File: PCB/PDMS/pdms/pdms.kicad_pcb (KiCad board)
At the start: 2 copper layers, 152 parts, among them IC1 BTS500101TAEATMA1, IC12 TMP126NDCKR, IC13 TMP126NDCKR, IC14 TMP126NDCKR, IC15 LM74700QDBVRQ1, IC16 BTS722204ESAXUMA1, IC2 BTS500101TAEATMA1, IC3 BTS500101TAEATMA1, IC4 BTS500101TAEATMA1, IC5 BTS500101TAEATMA1, IC6 BTS500101TAEATMA1, IC7 BTS722204ESAXUMA1, IC8 BTS500101TAEATMA1, IC9 BTS500101TAEATMA1, J1 DBG, Q1 AO3401A, Q2 MMBT3904, Q3 IAUA250N04S6N007AUMA1, U1 STM32F405RGTx, U2 MCP2561-E-SN, U3 MCP2561-E-SN, Y1 16Mhz, Y2 32KHz

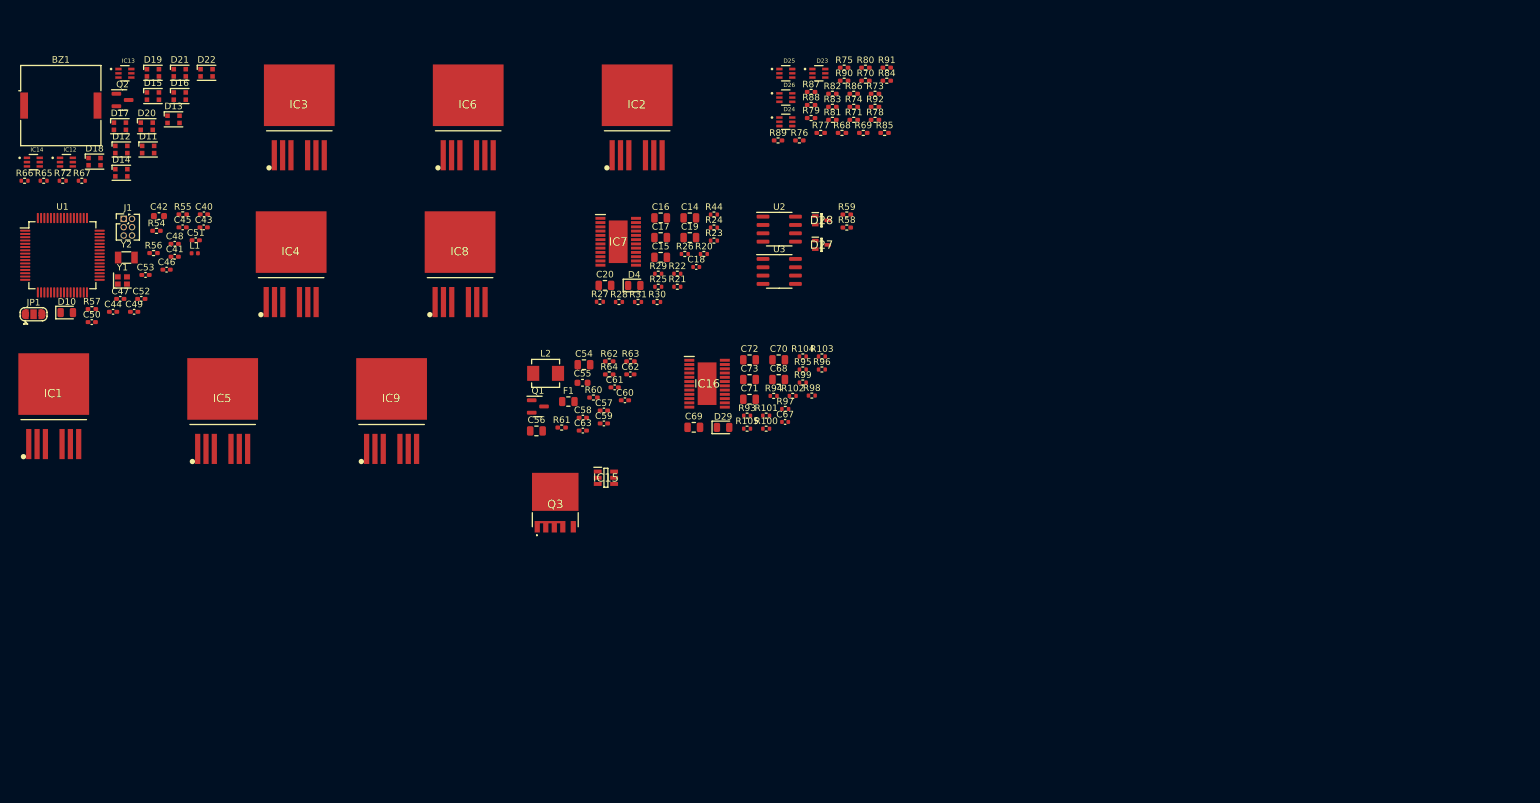
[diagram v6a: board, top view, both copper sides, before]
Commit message: Changed MCU to L496 & finished powerswitch section
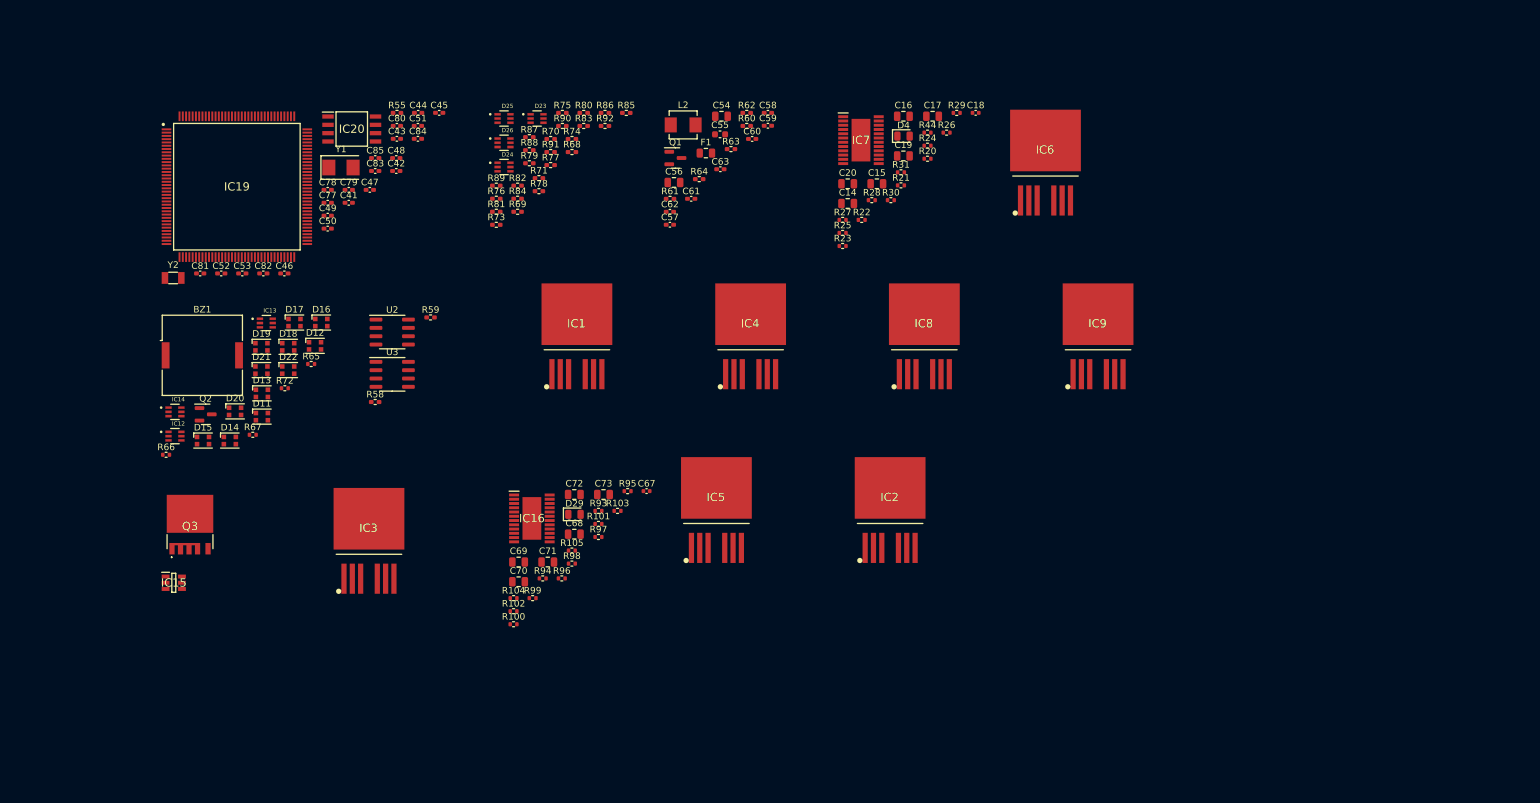
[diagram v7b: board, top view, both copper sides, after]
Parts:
- removed C40: 2u2, Capacitor_SMD:C_0402_1005Metric_Pad0.74x0.62mm_HandSolder
- removed D10: LED_Small, LED_SMD:LED_0805_2012Metric
- removed D27, D28: PESD2CANFD24L-UX, PDMS_Additional:SOT65P210X110-3N
- removed J1: DBG, Connector_PinHeader_1.27mm:PinHeader_2x03_P1.27mm_Vertical
- removed JP1: SolderJumper_3_Open, Jumper:SolderJumper-3_P1.3mm_Open_RoundedPad1.0x1.5mm
- removed L1: 2u7 120m, Inductor_SMD:L_0402_1005Metric
- removed R54: 2k2, Resistor_SMD:R_0402_1005Metric_Pad0.72x0.64mm_HandSolder
- removed R56: 1k5, Resistor_SMD:R_0402_1005Metric_Pad0.72x0.64mm_HandSolder
- removed R57: 1k, Resistor_SMD:R_0402_1005Metric_Pad0.72x0.64mm_HandSolder
- removed U1: STM32F405RGTx, Package_QFP:LQFP-64_10x10mm_P0.5mm
- added C77: 100n, Capacitor_SMD:C_0402_1005Metric_Pad0.74x0.62mm_HandSolder, F.Cu at (69.9, 42.8)
- added C78: 100n, Capacitor_SMD:C_0402_1005Metric_Pad0.74x0.62mm_HandSolder, F.Cu at (69.9, 40.8)
- added C79: 100n, Capacitor_SMD:C_0402_1005Metric_Pad0.74x0.62mm_HandSolder, F.Cu at (73.1, 40.8)
- added C80: 100n, Capacitor_SMD:C_0402_1005Metric_Pad0.74x0.62mm_HandSolder, F.Cu at (80.5, 31.0)
- added C81: 100n, Capacitor_SMD:C_0402_1005Metric_Pad0.74x0.62mm_HandSolder, F.Cu at (50.5, 53.5)
- added C82: 100n, Capacitor_SMD:C_0402_1005Metric_Pad0.74x0.62mm_HandSolder, F.Cu at (60.1, 53.5)
- added C83: 1u, Capacitor_SMD:C_0402_1005Metric_Pad0.74x0.62mm_HandSolder, F.Cu at (77.2, 37.9)
- added C84: 10pF, Capacitor_SMD:C_0402_1005Metric_Pad0.74x0.62mm_HandSolder, F.Cu at (83.7, 33.0)
- added C85: 10pF, Capacitor_SMD:C_0402_1005Metric_Pad0.74x0.62mm_HandSolder, F.Cu at (77.2, 36.0)
- added IC19: STM32L496ZGT6, PDM_Additional:QFP50P2200X2200X160-144N, F.Cu at (56.1, 40.3)
- added IC20: AT25SF128A-SHB-T, PDM_Additional:SOIC127P798X216-8N, F.Cu at (73.6, 31.5)
- C41: value 2u2 -> 4u7
- C42: value 4,7uF -> 10pF; footprint Capacitor_SMD:C_0603_1608Metric -> Capacitor_SMD:C_0402_1005Metric_Pad0.74x0.62mm_HandSolder
- C43: value 100nF -> 1u
- C44, C45: value 100nF -> 100n
- C46: value 100nF -> 10pF
- C48, C50, C52, C53: value 10pF -> 100n
- C51: value 1u -> 100n
- R55: value 2k2 -> 1k
- Y1: value 16Mhz -> 48Mhz; footprint Crystal:Crystal_SMD_2016-4Pin_2.0x1.6mm -> Crystal:Crystal_SMD_5032-2Pin_5.0x3.2mm
- moved IC9 108.4 mm to (187.4, 59.8)
- moved IC6 88.3 mm to (179.4, 33.3)
- moved IC1 80.5 mm to (107.9, 59.8)
- moved IC5 76.8 mm to (129.2, 86.3)
- moved R58 76.7 mm to (77.2, 73.2)
- moved IC8 71.7 mm to (160.9, 59.8)
- moved IC2 71.3 mm to (155.7, 86.3)
- moved IC4 70.9 mm to (134.4, 59.8)
- moved IC15 67.8 mm to (46.4, 100.7)
- moved IC3 65.5 mm to (76.2, 91.0)
- moved R59 65.4 mm to (85.6, 60.3)
- moved R73 61.1 mm to (95.6, 46.1)
- moved U2 61.1 mm to (79.8, 62.5)
- moved U3 61.1 mm to (79.8, 68.9)
- moved R84 59.1 mm to (98.9, 42.1)
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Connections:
- net /POWER_SWITCHES/BTS50010-1TAE/MOS_OUT renamed HP_MOS1
- net /POWER_SWITCHES/BTS50010-1TAE1/MOS_OUT renamed HP_MOS2
- net /POWER_SWITCHES/BTS50010-1TAE2/MOS_OUT renamed HP_MOS3
- net /POWER_SWITCHES/BTS50010-1TAE3/MOS_OUT renamed HP_MOS4
- net /POWER_SWITCHES/BTS50010-1TAE4/MOS_OUT renamed HP_MOS5
- net /POWER_SWITCHES/BTS50010-1TAE6/MOS_OUT renamed HP_MOS6
- net /POWER_SWITCHES/BTS722204/ADC renamed SENS_OUT_LP1
- net /POWER_SWITCHES/BTS722204/IN0 renamed LP_SIG_IN1
- net /POWER_SWITCHES/BTS722204/IN1 renamed LP_SIG_IN2
- net /POWER_SWITCHES/BTS722204/IN2 renamed LP_SIG_IN3
- net /POWER_SWITCHES/BTS722204/IN3 renamed LP_SIG_IN4
- net /POWER_SWITCHES/BTS722204/OUT0 renamed LP_MOS1
- net /POWER_SWITCHES/BTS722204/OUT1 renamed LP_MOS2
- net /POWER_SWITCHES/BTS722204/OUT2 renamed LP_MOS3
- net /POWER_SWITCHES/BTS722204/OUT3 renamed LP_MOS4
- net /POWER_SWITCHES/BTS722205/ADC renamed SENS_OUT_LP2
- net /POWER_SWITCHES/BTS722205/IN0 renamed LP_SIG_IN5
- net /POWER_SWITCHES/BTS722205/IN1 renamed LP_SIG_IN6
- net /POWER_SWITCHES/BTS722205/IN2 renamed LP_SIG_IN7
- net /POWER_SWITCHES/BTS722205/IN3 renamed LP_SIG_IN8
- net /POWER_SWITCHES/BTS722205/OUT0 renamed LP_MOS5
- net /POWER_SWITCHES/BTS722205/OUT1 renamed LP_MOS6
- net /POWER_SWITCHES/BTS722205/OUT2 renamed LP_MOS7
- net /POWER_SWITCHES/BTS722205/OUT3 renamed LP_MOS8
- C20 pad 2: /POWER_SWITCHES/BTS722204/VS -> +12V
- C41 pad 1: Net-(C41-Pad1) -> VDD
- C42 pad 1: +3.3V -> OSC_IN
- C43 pad 1: +3.3V -> VDDA
- C44 pad 1: +3.3V -> VDD
- C45 pad 1: +3.3V -> VDD
- C46 pad 1: +3.3V -> OSC_OUT
- C47 pad 1: +3.3V -> VDDA
- C48 pad 1: OSC_IN -> VDD
- C49 pad 1: +3.3VA -> VDD
- C50 pad 1: OSC_OUT -> VDD
- C51 pad 1: +3.3VA -> VDD
- C52 pad 1: OSC32_IN -> VDD
- C53 pad 1: OSC32_OUT -> VDD
- C61 pad 2: +3.3V -> VDD
- C62 pad 2: +3.3V -> VDD
- C63 pad 2: +3.3V -> VDD
- C69 pad 2: /POWER_SWITCHES/BTS722205/VS -> +12V
- D23 pad 4: +3.3V -> VDD
- D23 pad 5: +3.3V -> VDD
- D24 pad 3: ADC_PROT2 -> ADC_PROT4
- D24 pad 4: +3.3V -> VDD
- D24 pad 5: +3.3V -> VDD
- D24 pad 6: ADC_PROT1 -> ADC_PROT3
- D25 pad 3: ADC_PROT2 -> ADC_PROT6
- D25 pad 4: +3.3V -> VDD
- D25 pad 5: +3.3V -> VDD
- D25 pad 6: ADC_PROT1 -> ADC_PROT5
- D26 pad 3: ADC_PROT2 -> ADC_PROT8
- D26 pad 4: +3.3V -> VDD
- D26 pad 5: +3.3V -> VDD
- D26 pad 6: ADC_PROT1 -> ADC_PROT7
- IC12 pad 6: +3.3V -> VDD
- IC13 pad 6: +3.3V -> VDD
- IC14 pad 6: +3.3V -> VDD
- IC16 pad 25: /POWER_SWITCHES/BTS722205/VS -> +12V
- IC7 pad 25: /POWER_SWITCHES/BTS722204/VS -> +12V
- IC8 pad 5: /POWER_SWITCHES/BTS50010-1TAE7/MOS_OUT -> HP_MOS7
- IC8 pad 6: /POWER_SWITCHES/BTS50010-1TAE7/MOS_OUT -> HP_MOS7
- IC8 pad 7: /POWER_SWITCHES/BTS50010-1TAE7/MOS_OUT -> HP_MOS7
- IC9 pad 5: /POWER_SWITCHES/BTS50010-1TAE5/MOS_OUT -> HP_MOS7
- IC9 pad 6: /POWER_SWITCHES/BTS50010-1TAE5/MOS_OUT -> HP_MOS7
- IC9 pad 7: /POWER_SWITCHES/BTS50010-1TAE5/MOS_OUT -> HP_MOS7
- L2 pad 2: +3.3V -> VDD
- R29 pad 2: +3.3V -> VDD
- R55 pad 1: +3.3V -> BOOT0
- R55 pad 2: I2C2_SDA -> Net-(JP1-Pad2)
- R64 pad 1: +3.3V -> VDD
- R65 pad 1: +3.3V -> VDD
- R66 pad 1: +3.3V -> VDD
- R67 pad 2: +3.3V -> VDD
- R68 pad 2: /ADC_PROT/ADC1_IN1 -> ADC_IN1
- R70 pad 2: /ADC_PROT/ADC1_IN2 -> ADC_IN2
- R75 pad 2: /ADC_PROT/ADC1_IN1 -> ADC_IN3
- R77 pad 2: /ADC_PROT/ADC1_IN2 -> ADC_IN4
- R79 pad 2: /ADC_PROT/ADC1_IN1 -> ADC_IN5
- R81 pad 2: /ADC_PROT/ADC1_IN2 -> ADC_IN6
- R83 pad 2: /ADC_PROT/ADC1_IN1 -> ADC_IN7
- R85 pad 2: /ADC_PROT/ADC1_IN2 -> ADC_IN8
- R87 pad 2: ADC_PROT1 -> ADC_PROT3
- R88 pad 2: ADC_PROT2 -> ADC_PROT4
- R89 pad 2: ADC_PROT1 -> ADC_PROT5
- R90 pad 2: ADC_PROT2 -> ADC_PROT6
- R91 pad 2: ADC_PROT1 -> ADC_PROT7
- R92 pad 2: ADC_PROT2 -> ADC_PROT8
- R95 pad 2: +3.3V -> VDD
- Y1 pad 2: GND -> OSC_OUT

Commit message: Wired all peripherals
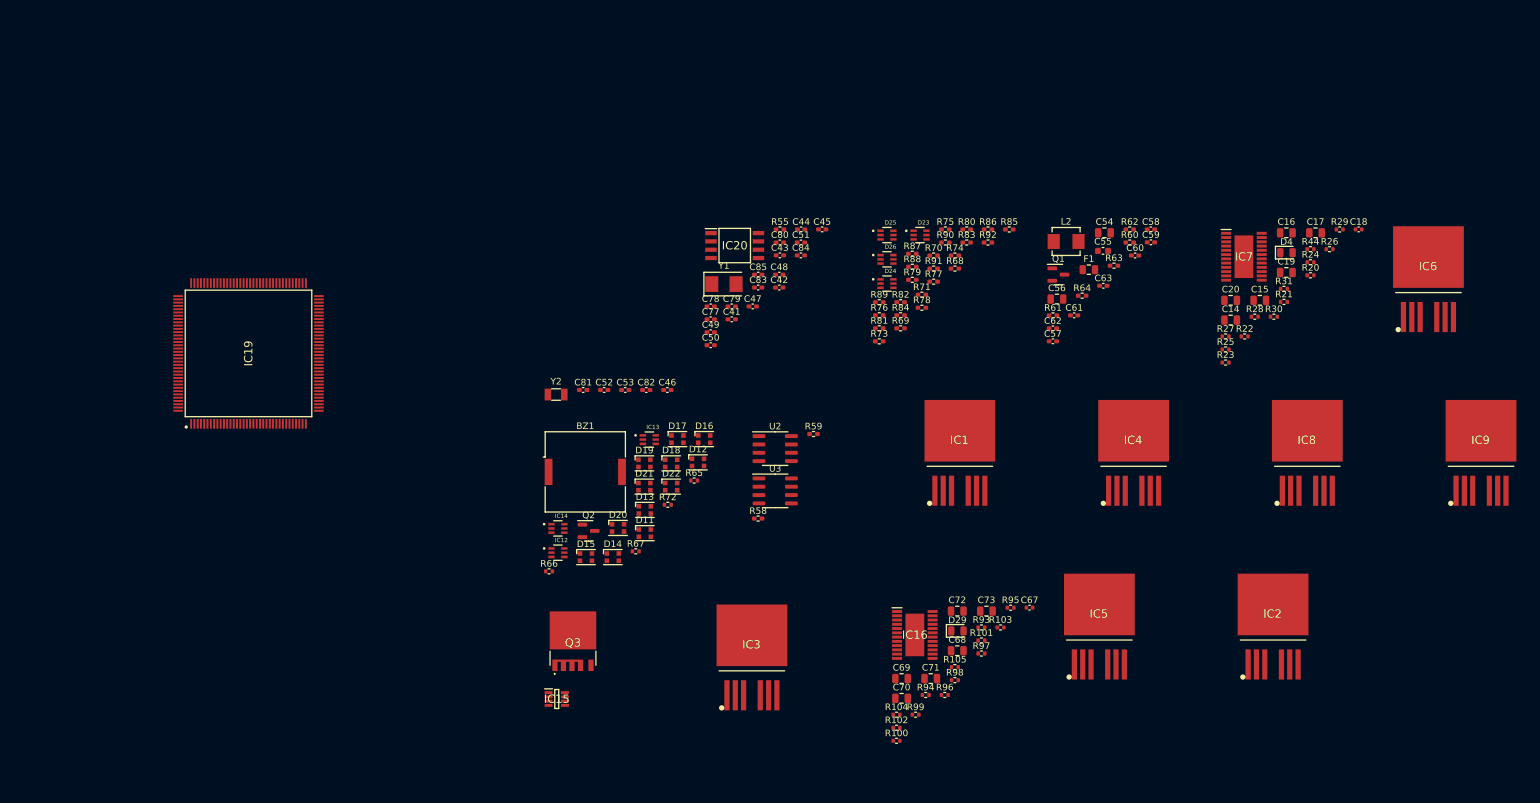
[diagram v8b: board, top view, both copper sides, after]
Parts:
- IC15: value LM74700QDBVRQ1 -> LM74700MDDFREP; footprint PDMS_Additional:SOT95P280X145-6N -> PDMS_Additional:SOT65P280X110-8N
- moved C15 61.1 mm to (212.1, 57.6)
- moved C17 61.1 mm to (220.6, 47.4)
- moved C18 61.1 mm to (227.2, 46.8)
- moved C43 61.1 mm to (138.9, 50.8)
- moved C44 61.1 mm to (142.1, 46.8)
- moved C58 61.1 mm to (195.5, 46.8)
- moved C59 61.1 mm to (195.5, 48.8)
- moved C63 61.1 mm to (188.2, 55.4)
- moved C67 61.1 mm to (177.0, 104.5)
- moved C80 61.1 mm to (138.9, 48.8)
- moved D24 61.1 mm to (155.2, 55.1)
- moved D25 61.1 mm to (155.2, 47.7)
- moved D26 61.1 mm to (155.2, 51.4)
- moved D29 61.1 mm to (166.0, 108.1)
- moved D4 61.1 mm to (216.2, 50.4)
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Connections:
- net /CAN_BUS1/CAN1_H renamed CAN1_H
- net /CAN_BUS1/CAN1_L renamed CAN1_L
- net /CAN_BUS1/CAN2_H renamed CAN2_H
- net /CAN_BUS1/CAN2_L renamed CAN2_L
- net /CSN_SECA5 renamed SIG_IN1
- net /CSN_SECA6 renamed SIG_IN2
- net /I2C1_SCL renamed /IMU/IMU_I2C_SCL
- net /I2C1_SDA renamed /IMU/IMU_I2C_SDA
- net /SENS_OUT1 renamed SENS_OUT1
- net /SENS_OUT2 renamed SENS_OUT2
- net /SENS_OUT3 renamed SENS_OUT3
- net /SENS_OUT4 renamed SENS_OUT4
- net /SENS_OUT5 renamed SENS_OUT5
- net /SENS_OUT6 renamed SENS_OUT6
- net /SENS_OUT7 renamed SENS_OUT7
- net /SENS_OUT8 renamed SENS_OUT8
- net CAN1_RX renamed /CAN_BUS/CAN1_RX
- net CAN1_TX renamed /CAN_BUS/CAN1_TX
- net TEMP2_ALERT renamed /PERIPHERAL/TEMP2_ALERT
- IC12 pad 1: TEMP1_CS -> /PERIPHERAL/TEMP1_CS
- IC12 pad 3: SPI2_IO -> MISO
- IC12 pad 4: SPI2_CLK -> SCK
- IC12 pad 5: TEMP1_ALERT -> /PERIPHERAL/TEMP1_ALERT
- IC14 pad 1: TEMP2_CS -> /PERIPHERAL/TEMP2_CS
- IC14 pad 3: SPI2_IO -> MISO
- IC14 pad 4: SPI2_CLK -> SCK
- IC15 pad 1: Net-(C65-Pad1) -> /REVERSE_POLARITY_PROT/IN
- IC15 pad 3: /REVERSE_POLARITY_PROT/IN -> unconnected-(IC15-Pad3)
- IC15 pad 4: +12V -> Net-(C65-Pad2)
- IC15 pad 5: Net-(IC15-Pad5) -> /REVERSE_POLARITY_PROT/IN
- IC15 pad 6: /REVERSE_POLARITY_PROT/IN -> Net-(Q3-Pad5)
- IC19 pad 111: /SCK -> SCK
- IC19 pad 112: /MISO -> MISO
- IC19 pad 113: /MOSI -> MOSI
- IC19 pad 115: /SCK -> /PERIPHERAL/TEMP1_CS
- IC19 pad 116: unconnected-(IC19-Pad116) -> /PERIPHERAL/TEMP2_CS
- IC19 pad 117: /MISO -> unconnected-(IC19-Pad117)
- IC19 pad 118: /MOSI -> unconnected-(IC19-Pad118)
- IC19 pad 12: unconnected-(IC19-Pad12) -> /NTC_SECTION/NTC_SEL1
- IC19 pad 124: unconnected-(IC19-Pad124) -> /IMU/IMU_INT2
- IC19 pad 125: unconnected-(IC19-Pad125) -> /IMU/IMU_INT1
- IC19 pad 126: unconnected-(IC19-Pad126) -> /IMU/IMU_I2C_SA0
- IC19 pad 127: unconnected-(IC19-Pad127) -> /IMU/IMU_MODE_SEL
- IC19 pad 13: SENS_OUT_LP1 -> /NTC_SECTION/NTC_SEL2
- IC19 pad 135: /PWM_OUT2 -> /CAN_BUS/CAN2_RX
- IC19 pad 136: /PWM_OUT1 -> /CAN_BUS/CAN2_TX
- IC19 pad 14: SENS_OUT_LP2 -> /NTC_SECTION/NTC_SEL3
- IC19 pad 15: unconnected-(IC19-Pad15) -> /NTC_SECTION/NTC_ADC
- IC19 pad 18: unconnected-(IC19-Pad18) -> SENS_OUT_LP1
- IC19 pad 19: unconnected-(IC19-Pad19) -> SENS_OUT_LP2
- IC19 pad 53: unconnected-(IC19-Pad53) -> LP_SIG_IN1
- IC19 pad 54: unconnected-(IC19-Pad54) -> LP_SIG_IN2
- IC19 pad 55: unconnected-(IC19-Pad55) -> LP_SIG_IN3
- IC19 pad 56: unconnected-(IC19-Pad56) -> LP_SIG_IN4
- IC19 pad 57: unconnected-(IC19-Pad57) -> LP_SIG_IN5
- IC19 pad 58: unconnected-(IC19-Pad58) -> LP_SIG_IN6
- IC19 pad 59: unconnected-(IC19-Pad59) -> LP_SIG_IN7
- IC19 pad 60: unconnected-(IC19-Pad60) -> LP_SIG_IN8
- IC19 pad 73: CAN2_RX -> unconnected-(IC19-Pad73)
- IC19 pad 74: CAN2_TX -> SCK
- IC19 pad 75: unconnected-(IC19-Pad75) -> MISO
- IC19 pad 76: unconnected-(IC19-Pad76) -> MOSI
- IC19 pad 77: /CSN_SECA1 -> LP_CSN1
- IC19 pad 78: /CSN_SECA2 -> LP_CSN2
- IC19 pad 79: /CSN_SECA3 -> unconnected-(IC19-Pad79)
- IC19 pad 80: /CSN_SECA4 -> unconnected-(IC19-Pad80)
- IC19 pad 85: unconnected-(IC19-Pad85) -> SIG_IN3
- IC19 pad 86: unconnected-(IC19-Pad86) -> SIG_IN4
- IC19 pad 87: /SCK -> SCK
- IC19 pad 88: /MISO -> MISO
- IC19 pad 89: /MOSI -> MOSI
- IC19 pad 96: unconnected-(IC19-Pad96) -> SIG_IN5
- IC19 pad 97: unconnected-(IC19-Pad97) -> SIG_IN6
- IC19 pad 98: unconnected-(IC19-Pad98) -> SIG_IN7
- IC19 pad 99: unconnected-(IC19-Pad99) -> SIG_IN8
- Q3 pad 5: Net-(IC15-Pad5) -> Net-(Q3-Pad5)
- R100 pad 2: TB -> LP_CSN2
- R20 pad 2: SPI1_MISO -> MISO
- R21 pad 2: SPI1_MOSI -> MOSI
- R22 pad 2: SPI1_SCK -> SCK
- R23 pad 2: TB -> LP_CSN1
- R65 pad 2: TEMP1_ALERT -> /PERIPHERAL/TEMP1_ALERT
- R97 pad 2: SPI1_MISO -> MISO
- R98 pad 2: SPI1_MOSI -> MOSI
- R99 pad 2: SPI1_SCK -> SCK
- U3 pad 1: CAN2_TX -> /CAN_BUS/CAN2_TX
- U3 pad 4: CAN2_RX -> /CAN_BUS/CAN2_RX
